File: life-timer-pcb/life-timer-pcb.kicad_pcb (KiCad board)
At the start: 2 copper layers, 39 x 30.8 mm, 18 parts, among them J1 SSD1306_Socket, SW1 SW_RST, SW2 SW_Push, SW3 SW_Push, SW4 SW_Push, SW5 SW_PWR, U1 ATtiny85-20S

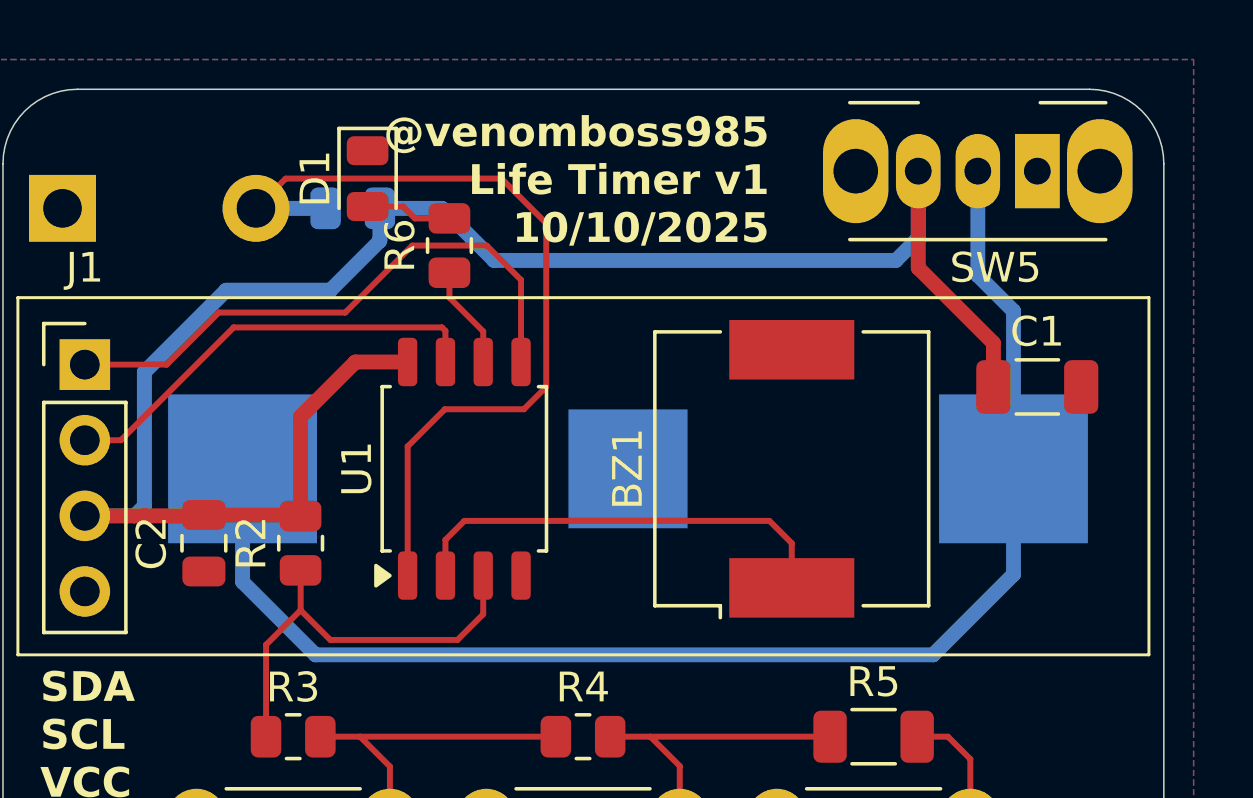
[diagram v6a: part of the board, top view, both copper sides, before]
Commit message: User LED moved for better layout; passes DRC
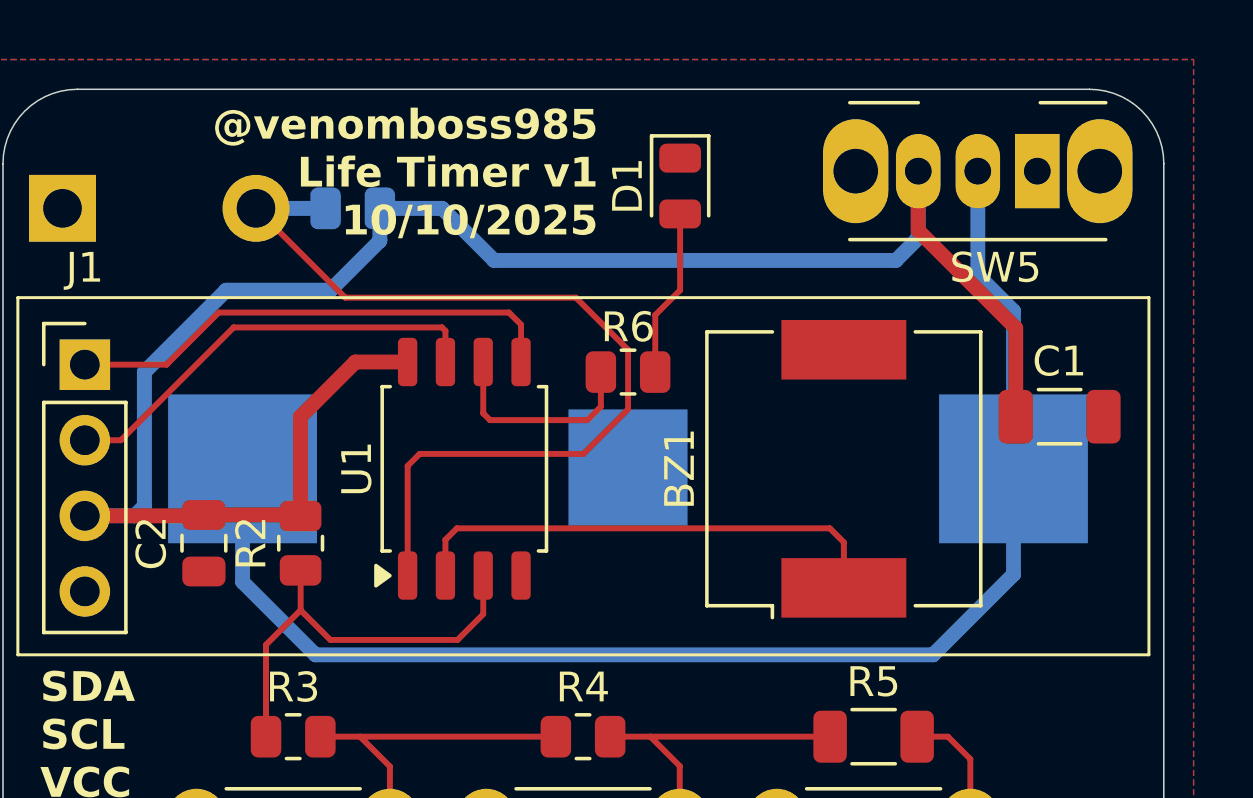
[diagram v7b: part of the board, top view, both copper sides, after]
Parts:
- moved D1 10.5 mm to (149.8, 89.2)
- moved R6 7.35 mm to (148.0, 95.5), turned to 0 degrees
- moved BZ1 1.75 mm to (155.2, 98.8)
- moved C1 1.25 mm to (162.5, 97.0)
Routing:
- net Net-(U1-PB1): track 3.47 -> 7.12 mm
- net Net-(D1-A): track 2.92 -> 5.66 mm
- net SDA: track 19.5 -> 16.8 mm
- net ~{RESET}: track 28.4 -> 30.7 mm
- net Net-(BZ1-+): track 14.9 -> 16.5 mm
- net VCC: track 62.1 -> 63.4 mm
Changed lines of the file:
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@@
 	(footprint "Resistor_SMD:R_0805_2012Metric"
 		(layer "F.Cu")
-		(at 142 91.25 90)
+		(at 148 95.5)
 		(descr "Resistor SMD 0805 (2012 Metric), square (rectangular) end terminal, IPC-7351 nominal, (Body size source: IPC-SM-782 page 72, https://www.pcb-3d.com/wordpress/wp-content/uploads/ipc-sm-782a_amendment_1_and_2.pdf), generated with kicad-footprint-generator")
 		(tags "resistor")
 		(property "Reference" "R6"
-			(at 0 -1.65 90)
+			(at 0 -1.5 0)
 			(layer "F.SilkS")
 			(effects
@@
 		)
 		(property "Value" "680"
-			(at 0 1.65 90)
+			(at 0 1.65 0)
 			(layer "F.Fab")
 			(effects
@@
 		)
 		(property "Datasheet" "~"
-			(at 0 0 90)
+			(at 0 0 0)
 			(layer "F.Fab")
 			(hide yes)
@@
 		)
 		(property "Description" "Resistor, small US symbol"
-			(at 0 0 90)
+			(at 0 0 0)
 			(layer "F.Fab")
 			(hide yes)
@@
 		)
 		(fp_line
-			(start 1.68 -0.95)
-			(end 1.68 0.95)
+			(start -1.68 -0.95)
+			(end 1.68 -0.95)
 			(stroke
 				(width 0.05)
@@
 		)
 		(fp_line
-			(start -1.68 -0.95)
-			(end 1.68 -0.95)
+			(start -1.68 0.95)
+			(end -1.68 -0.95)
 			(stroke
 				(width 0.05)
@@
 		)
 		(fp_line
-			(start 1.68 0.95)
-			(end -1.68 0.95)
+			(start 1.68 -0.95)
+			(end 1.68 0.95)
 			(stroke
 				(width 0.05)
@@
 		)
 		(fp_line
-			(start -1.68 0.95)
-			(end -1.68 -0.95)
+			(start 1.68 0.95)
+			(end -1.68 0.95)
 			(stroke
 				(width 0.05)
@@
 		)
 		(fp_line
-			(start 1 -0.625)
-			(end 1 0.625)
+			(start -1 -0.625)
+			(end 1 -0.625)
 			(stroke
 				(width 0.1)
@@
 		)
 		(fp_line
-			(start -1 -0.625)
-			(end 1 -0.625)
+			(start -1 0.625)
+			(end -1 -0.625)
 			(stroke
 				(width 0.1)
@@
 		)
 		(fp_line
-			(start 1 0.625)
-			(end -1 0.625)
+			(start 1 -0.625)
+			(end 1 0.625)
 			(stroke
 				(width 0.1)
@@
 		)
 		(fp_line
-			(start -1 0.625)
-			(end -1 -0.625)
+			(start 1 0.625)
+			(end -1 0.625)
 			(stroke
 				(width 0.1)
@@
 		)
 		(fp_text user "${REFERENCE}"
-			(at 0 0 90)
+			(at 0 0 0)
 			(layer "F.Fab")
 			(effects
@@
 		)
 		(pad "1" smd roundrect
-			(at -0.9125 0 90)
+			(at -0.9125 0)
 			(size 1.025 1.4)
 			(layers "F.Cu" "F.Mask" "F.Paste")
@@
 		)
 		(pad "2" smd roundrect
-			(at 0.9125 0 90)
+			(at 0.9125 0)
 			(size 1.025 1.4)
 			(layers "F.Cu" "F.Mask" "F.Paste")
@@
 	(footprint "LED_SMD:LED_0805_2012Metric"
 		(layer "F.Cu")
-		(at 139.25 89 -90)
+		(at 149.75 89.25 -90)
 		(descr "LED SMD 0805 (2012 Metric), square (rectangular) end terminal, IPC-7351 nominal, (Body size source: https://docs.google.com/spreadsheets/d/1BsfQQcO9C6DZCsRaXUlFlo91Tg2WpOkGARC1WS5S8t0/edit?usp=sharing), generated with kicad-footprint-generator")
 		(tags "LED")
@@
 	(footprint "Buzzer_Beeper:Buzzer_CUI_CPT-9019S-SMT"
 		(layer "F.Cu")
-		(at 153.5 98.75 90)
+		(at 155.25 98.75 90)
 		(descr "https://www.cui.com/product/resource/cpt-9019s-smt.pdf")
 		(tags "buzzer piezo")
@@
 	(footprint "Capacitor_SMD:C_1206_3216Metric"
 		(layer "F.Cu")
-		(at 161.75 96)
+		(at 162.5 97)
 		(descr "Capacitor SMD 1206 (3216 Metric), square (rectangular) end terminal, IPC-7351 nominal, (Body size source: IPC-SM-782 page 76, https://www.pcb-3d.com/wordpress/wp-content/uploads/ipc-sm-782a_amendment_1_and_2.pdf), generated with kicad-footprint-generator")
 		(tags "capacitor")
@@
 	)
 	(gr_text "@venomboss985\nLife Timer v1\n10/10/2025"
-		(at 152.75 91.25 0)
+		(at 147 91 0)
 		(layer "F.SilkS")
 		(effects
@@
 	)
 	(segment
-		(start 160.275 96)
-		(end 160.275 94.525)
+		(start 157.75 90.75)
+		(end 161.025 94.025)
 		(width 0.5)
 		(layer "F.Cu")
@@
 	)
 	(segment
-		(start 160.275 94.525)
-		(end 157.75 92)
+		(start 140.595 95.1625)
+		(end 138.8375 95.1625)
 		(width 0.5)
 		(layer "F.Cu")
@@
 	)
 	(segment
-		(start 140.595 95.1625)
-		(end 138.8375 95.1625)
+		(start 137 97)
+		(end 137 100.3375)
 		(width 0.5)
 		(layer "F.Cu")
@@
 	)
 	(segment
-		(start 137 97)
-		(end 137 100.3375)
+		(start 161.025 94.025)
+		(end 161.025 97)
 		(width 0.5)
 		(layer "F.Cu")
@@
 	)
 	(segment
-		(start 157.75 92)
-		(end 157.75 88.75)
+		(start 157.75 88.75)
+		(end 157.75 90.75)
 		(width 0.5)
 		(layer "F.Cu")
@@
 	(segment
 		(start 141.865 101.135)
-		(end 142.5 100.5)
+		(end 142.25 100.75)
 		(width 0.2)
 		(layer "F.Cu")
@@
 	)
 	(segment
-		(start 142.5 100.5)
-		(end 152.75 100.5)
+		(start 141.865 102.3375)
+		(end 141.865 101.135)
 		(width 0.2)
 		(layer "F.Cu")
@@
 	)
 	(segment
-		(start 153.5 101.25)
-		(end 153.5 102.75)
+		(start 154.780979 100.75)
+		(end 155.25 101.219021)
 		(width 0.2)
 		(layer "F.Cu")
@@
 	)
 	(segment
-		(start 141.865 102.3375)
-		(end 141.865 101.135)
+		(start 155.25 101.219021)
+		(end 155.25 102.75)
 		(width 0.2)
 		(layer "F.Cu")
@@
 	)
 	(segment
-		(start 152.75 100.5)
-		(end 153.5 101.25)
+		(start 142.25 100.75)
+		(end 154.780979 100.75)
 		(width 0.2)
 		(layer "F.Cu")
@@
 	)
 	(segment
-		(start 143.25 91.25)
-		(end 144.405 92.405)
+		(start 134.25 93.5)
+		(end 144 93.5)
 		(width 0.2)
 		(layer "F.Cu")
@@
 	)
 	(segment
-		(start 140.75 91.25)
-		(end 143.25 91.25)
+		(start 144.405 93.905)
+		(end 144.405 95.1625)
 		(width 0.2)
 		(layer "F.Cu")
@@
 	)
 	(segment
-		(start 132.5 95.25)
-		(end 134.25 93.5)
+		(start 144 93.5)
+		(end 144.405 93.905)
 		(width 0.2)
 		(layer "F.Cu")
@@
 	)
 	(segment
-		(start 134.25 93.5)
-		(end 138.5 93.5)
-		(width 0.2)
-		(layer "F.Cu")
-		(net 5)
-	)
-	(segment
-		(start 144.405 92.405)
-		(end 144.405 95.1625)
-		(width 0.2)
-		(layer "F.Cu")
-		(net 5)
-	)
-	(segment
-		(start 138.5 93.5)
-		(end 140.75 91.25)
+		(start 132.5 95.25)
+		(end 134.25 93.5)
 		(width 0.2)
 		(layer "F.Cu")
@@
 	)
 	(segment
-		(start 143.75 89)
-		(end 136.5 89)
+		(start 146.25 93)
+		(end 138.5 93)
 		(width 0.2)
 		(layer "F.Cu")
@@
 	(segment
 		(start 140.595 102.3375)
-		(end 140.595 98)
+		(end 140.595 98.655)
 		(width 0.2)
 		(layer "F.Cu")
@@
 	)
 	(segment
-		(start 145.25 96)
-		(end 145.25 90.5)
+		(start 140.595 98.655)
+		(end 141 98.25)
 		(width 0.2)
 		(layer "F.Cu")
@@
 	)
 	(segment
-		(start 136.5 89)
-		(end 135.5 90)
+		(start 148 94.75)
+		(end 146.25 93)
 		(width 0.2)
 		(layer "F.Cu")
@@
 	)
 	(segment
-		(start 141.845 96.75)
-		(end 144.5 96.75)
+		(start 146.5 98.25)
+		(end 148 96.75)
 		(width 0.2)
 		(layer "F.Cu")
@@
 	)
 	(segment
-		(start 144.5 96.75)
-		(end 145.25 96)
+		(start 141 98.25)
+		(end 146.5 98.25)
 		(width 0.2)
 		(layer "F.Cu")
@@
 	)
 	(segment
-		(start 145.25 90.5)
-		(end 143.75 89)
+		(start 138.5 93)
+		(end 135.5 90)
 		(width 0.2)
 		(layer "F.Cu")
@@
 	)
 	(segment
-		(start 140.595 98)
-		(end 141.845 96.75)
+		(start 148 96.75)
+		(end 148 94.75)
 		(width 0.2)
 		(layer "F.Cu")
@@
 	)
 	(segment
-		(start 140.8375 90.3375)
-		(end 140.4375 89.9375)
+		(start 149.75 92.75)
+		(end 149.75 90.1875)
 		(width 0.2)
 		(layer "F.Cu")
@@
 	)
 	(segment
-		(start 142 90.3375)
-		(end 140.8375 90.3375)
+		(start 148.9125 93.5875)
+		(end 149.75 92.75)
 		(width 0.2)
 		(layer "F.Cu")
@@
 	)
 	(segment
-		(start 140.4375 89.9375)
-		(end 139.25 89.9375)
+		(start 148.9125 95.5)
+		(end 148.9125 93.5875)
 		(width 0.2)
 		(layer "F.Cu")
@@
 	)
 	(segment
-		(start 143.135 95.1625)
-		(end 143.135 94.135)
+		(start 143.364514 97.114514)
+		(end 146.635486 97.114514)
 		(width 0.2)
 		(layer "F.Cu")
@@
 	)
 	(segment
-		(start 142 93)
-		(end 142 92.1625)
+		(start 146.635486 97.114514)
+		(end 147.0875 96.6625)
 		(width 0.2)
 		(layer "F.Cu")
@@
 	)
 	(segment
-		(start 143.135 94.135)
-		(end 142 93)
+		(start 143.135 96.885)
+		(end 143.364514 97.114514)
+		(width 0.2)
+		(layer "F.Cu")
+		(net 14)
+	)
+	(segment
+		(start 147.0875 96.6625)
+		(end 147.0875 95.5)
+		(width 0.2)
+		(layer "F.Cu")
+		(net 14)
+	)
+	(segment
+		(start 143.135 95.1625)
+		(end 143.135 96.885)
 		(width 0.2)
 		(layer "F.Cu")

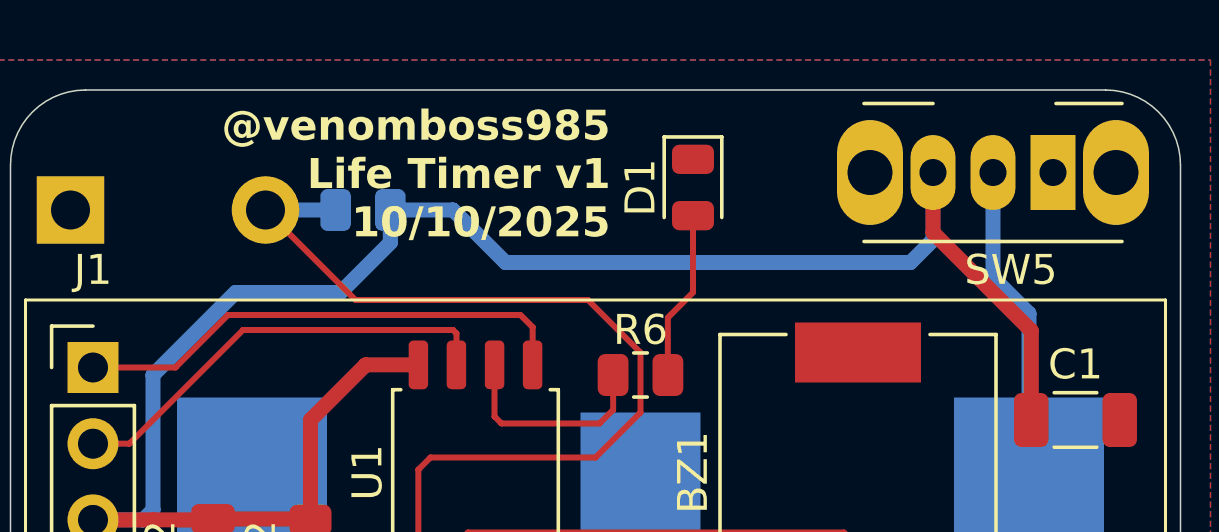
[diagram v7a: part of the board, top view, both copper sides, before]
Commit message: Added power indicator LED (might want to swap places in layout); passes ERC/DRC
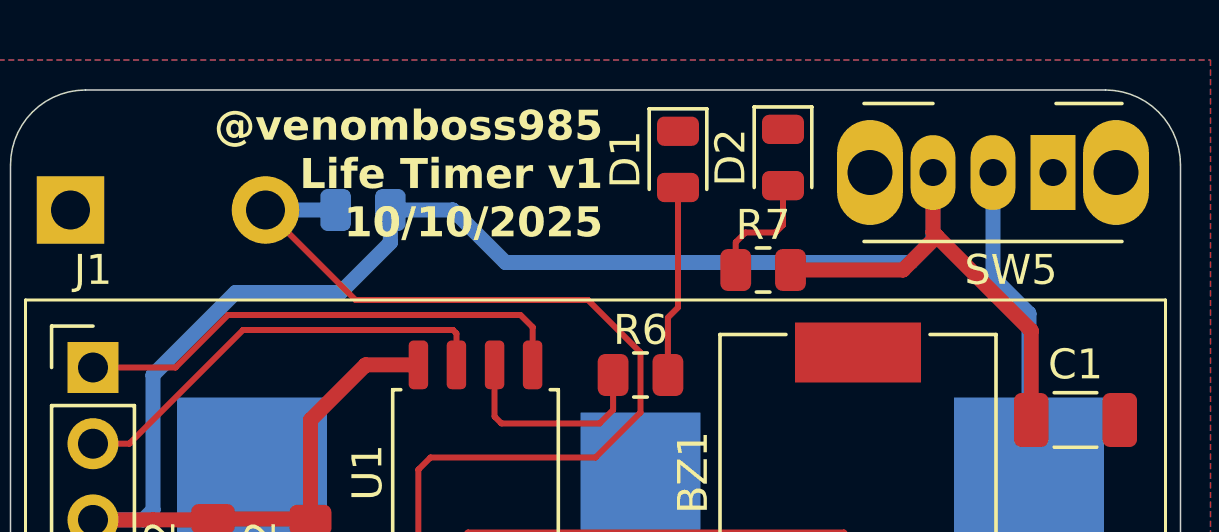
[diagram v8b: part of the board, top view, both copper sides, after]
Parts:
- added D2: RED, LED_SMD:LED_0805_2012Metric, F.Cu at (152.8, 88.2)
- added R7: 680, Resistor_SMD:R_0805_2012Metric, F.Cu at (152.1, 92.0)
- moved D1 1.06 mm to (149.2, 88.3)
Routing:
- net VCC: track 63.4 -> 68.8 mm
- net Net-(D2-A): track 0.00 -> 4.05 mm
- net Net-(D1-A): track 5.66 -> 6.39 mm
